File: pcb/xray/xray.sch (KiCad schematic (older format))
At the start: 5 parts, among them J1 Raspberry_Pi_2_3, M1 Nema17

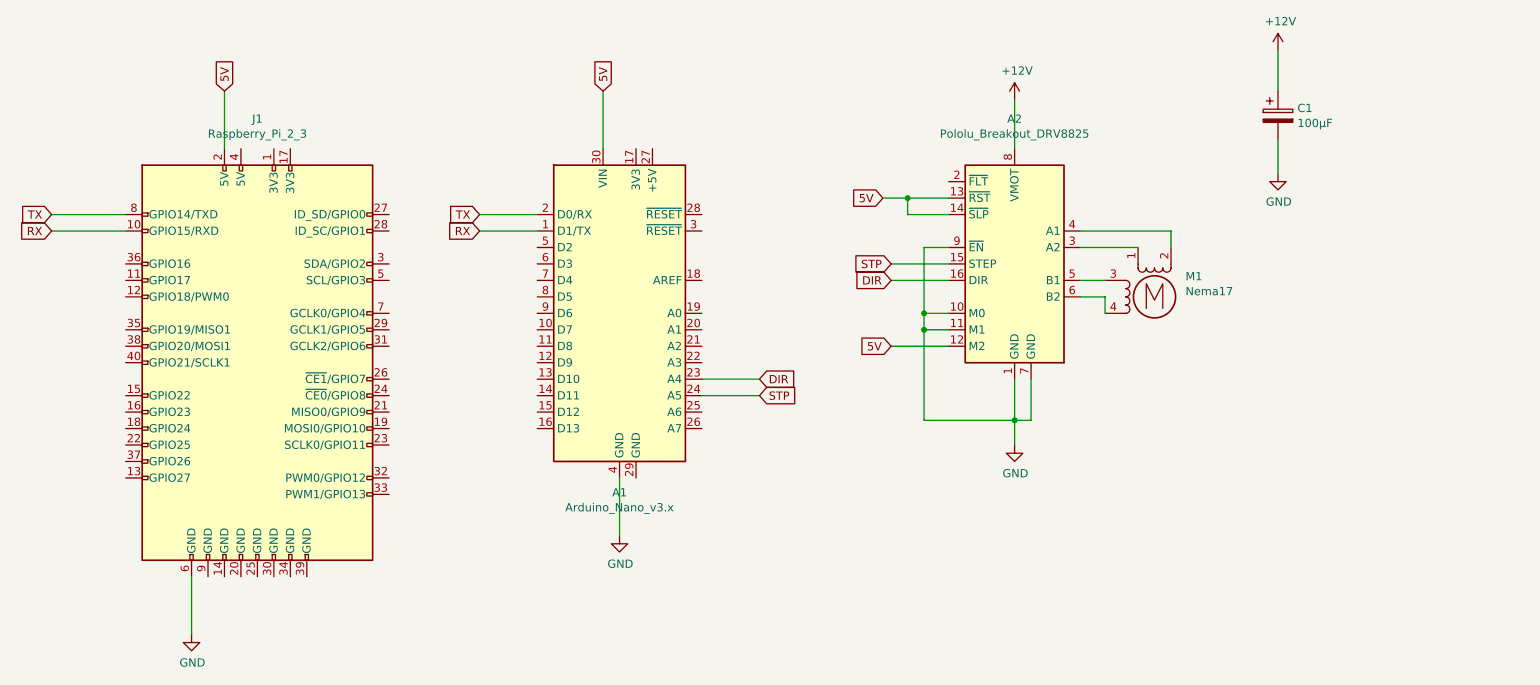
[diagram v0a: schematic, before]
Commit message: Add Schematic
Updated schematic using an Arduino pro micro or Leonardo
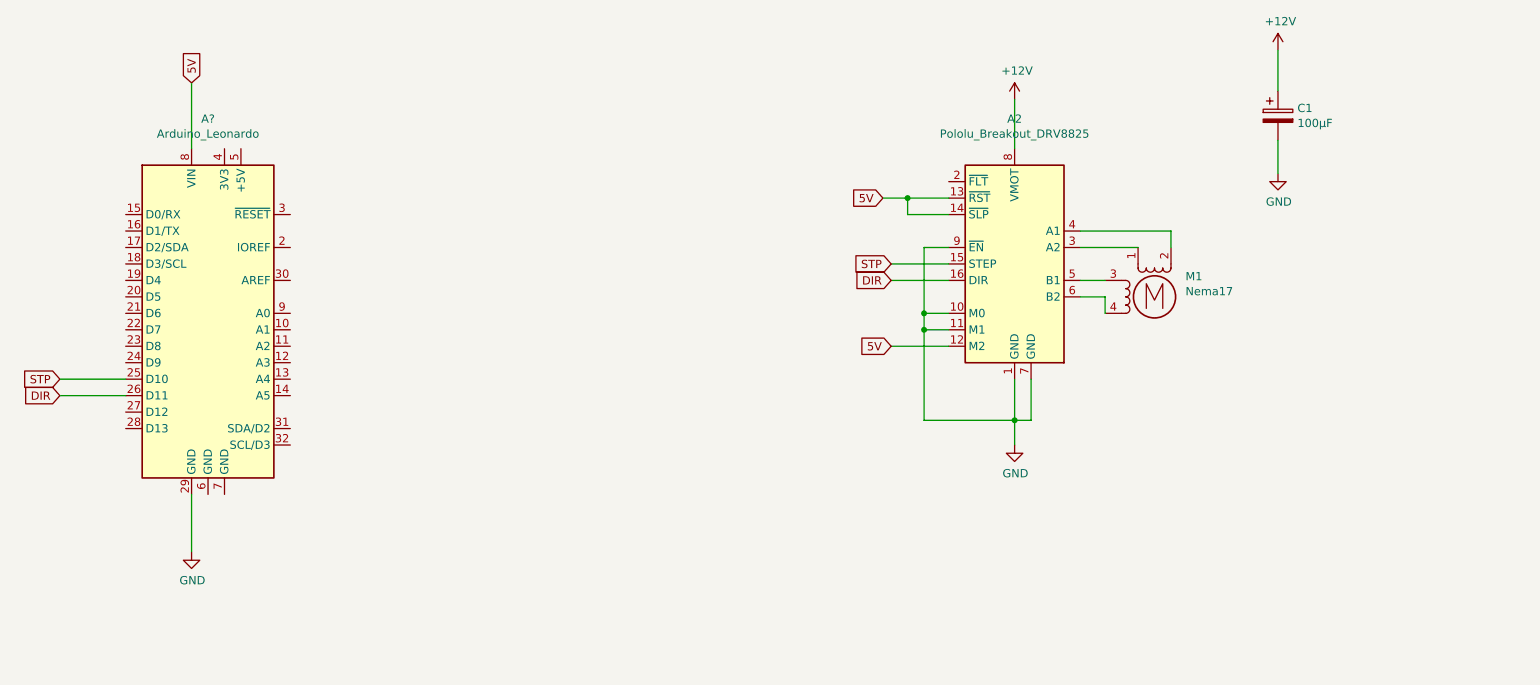
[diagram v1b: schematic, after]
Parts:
- removed A1: Arduino_Nano_v3.x, Module:Arduino_Nano, symbol MCU_Module:Arduino_Nano_v3.x
- removed J1: Raspberry_Pi_2_3, symbol Connector:Raspberry_Pi_2_3
- added A?: Arduino_Leonardo, Module:Arduino_UNO_R3, symbol MCU_Module:Arduino_Leonardo
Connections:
- net 5V: now also A?.8 (VIN)
- net DIR: now also A?.26 (D11)
- net GND: now also A?.29 (GND)
- net STP: now also A?.25 (D10)
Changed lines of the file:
@@
 $EndDescr
-$Comp
-L MCU_Module:Arduino_Nano_v3.x A1
-U 1 1 5E1B5952
-P 4400 2400
-F 0 "A1" H 4400 1311 50  0000 C CNN
-F 1 "Arduino_Nano_v3.x" H 4400 1220 50  0000 C CNN
-F 2 "Module:Arduino_Nano" H 4400 2400 50  0001 C CIN
-F 3 "http://www.mouser.com/pdfdocs/Gravitech_Arduino_Nano3_0.pdf" H 4400 2400 50  0001 C CNN
-	1    4400 2400
-	1    0    0    -1
-$EndComp
-$Comp
-L Connector:Raspberry_Pi_2_3 J1
-U 1 1 5E1B8D85
-P 2200 2700
-F 0 "J1" H 2200 4181 50  0000 C CNN
-F 1 "Raspberry_Pi_2_3" H 2200 4090 50  0000 C CNN
-F 2 "" H 2200 2700 50  0001 C CNN
-F 3 "https://www.raspberrypi.org/documentation/hardware/raspberrypi/schematics/rpi_SCH_3bplus_1p0_reduced.pdf" H 2200 2700 50  0001 C CNN
-	1    2200 2700
-	1    0    0    -1
-$EndComp
 $Comp
 L Device:CP C1
@@
 	1    0    0    -1
 $EndComp
-Text GLabel 2000 1050 1    50   Input ~ 0
-5V
-Text GLabel 950  1800 0    50   Input ~ 0
-TX
-Text GLabel 950  1900 0    50   Input ~ 0
-RX
-Wire Wire Line
-	2000 1400 2000 1050
-Wire Wire Line
-	1400 1800 950  1800
-Wire Wire Line
-	1800 4350 1800 4000
-$Comp
-L power:GND #PWR?
-U 1 1 5E21297F
-P 1800 4350
-F 0 "#PWR?" H 1800 4100 50  0001 C CNN
-F 1 "GND" H 1805 4177 50  0000 C CNN
-F 2 "" H 1800 4350 50  0001 C CNN
-F 3 "" H 1800 4350 50  0001 C CNN
-	1    1800 4350
-	1    0    0    -1
-$EndComp
-$Comp
-L power:GND #PWR?
-U 1 1 5E214FEC
-P 4400 3750
-F 0 "#PWR?" H 4400 3500 50  0001 C CNN
-F 1 "GND" H 4405 3577 50  0000 C CNN
-F 2 "" H 4400 3750 50  0001 C CNN
-F 3 "" H 4400 3750 50  0001 C CNN
-	1    4400 3750
-	1    0    0    -1
-$EndComp
-Wire Wire Line
-	4400 3750 4400 3400
-Text GLabel 4300 1050 1    50   Input ~ 0
-5V
-Text GLabel 3550 1900 0    50   Input ~ 0
-RX
-Text GLabel 3550 1800 0    50   Input ~ 0
-TX
-Wire Wire Line
-	4300 1050 4300 1400
 $Comp
 L power:GND #PWR?
@@
 	1    0    0    -1
 $EndComp
-Wire Wire Line
-	950  1900 1400 1900
-Wire Wire Line
-	3550 1900 3900 1900
-Wire Wire Line
-	3550 1800 3900 1800
-Text GLabel 5250 2800 2    50   Input ~ 0
-DIR
-Text GLabel 5250 2900 2    50   Input ~ 0
-STP
-Wire Wire Line
-	4900 2800 5250 2800
-Wire Wire Line
-	5250 2900 4900 2900
 Text GLabel 6050 2200 0    50   Input ~ 0
 DIR
@@
 Wire Wire Line
 	7750 1900 7200 1900
+$Comp
+L MCU_Module:Arduino_Leonardo A?
+U 1 1 5E1C1CEB
+P 1900 2400
+F 0 "A?" H 1900 3581 50  0000 C CNN
+F 1 "Arduino_Leonardo" H 1900 3490 50  0000 C CNN
+F 2 "Module:Arduino_UNO_R3" H 1900 2400 50  0001 C CIN
+F 3 "https://www.arduino.cc/en/Main/ArduinoBoardLeonardo" H 1900 2400 50  0001 C CNN
+	1    1900 2400
+	1    0    0    -1
+$EndComp
+Text GLabel 1800 1000 1    50   Input ~ 0
+5V
+$Comp
+L power:GND #PWR?
+U 1 1 5E1C79C8
+P 1800 3850
+F 0 "#PWR?" H 1800 3600 50  0001 C CNN
+F 1 "GND" H 1805 3677 50  0000 C CNN
+F 2 "" H 1800 3850 50  0001 C CNN
+F 3 "" H 1800 3850 50  0001 C CNN
+	1    1800 3850
+	1    0    0    -1
+$EndComp
+Text GLabel 1000 2900 0    50   Input ~ 0
+DIR
+Text GLabel 1000 2800 0    50   Input ~ 0
+STP
+Wire Wire Line
+	1000 2800 1400 2800
+Wire Wire Line
+	1400 2900 1000 2900
+Wire Wire Line
+	1800 3850 1800 3500
+Wire Wire Line
+	1800 1000 1800 1400
 $EndSCHEMATC

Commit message: Update schematic
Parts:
- removed A?: Arduino_Leonardo, Module:Arduino_UNO_R3, symbol MCU_Module:Arduino_Leonardo
- added MCU1: Arduino_Micro, xray:Arduino_Micro, symbol xray:Arduino_Micro
- C1: footprint (none) -> Capacitor_THT:C_Radial_D5.0mm_H11.0mm_P2.00mm
- M1: footprint (none) -> Connector_PinHeader_2.54mm:PinHeader_1x04_P2.54mm_Vertical
- renumbered A2 to StepperDriver1
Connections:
- net 5V: now also MCU1.12 (5V)
- net DIR: now also MCU1.8 (PF1)
- net GND: now also MCU1.14 (GND)
- net STP: now also MCU1.9 (PF0)
- no-connect marks 0 -> 29
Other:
- moved on the sheet: C1
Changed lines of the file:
@@
 L Device:CP C1
 U 1 1 5E1C1B73
-P 8400 1200
-F 0 "C1" H 8518 1246 50  0000 L CNN
-F 1 "100µF" H 8518 1155 50  0000 L CNN
-F 2 "" H 8438 1050 50  0001 C CNN
-F 3 "~" H 8400 1200 50  0001 C CNN
-	1    8400 1200
-	1    0    0    -1
-$EndComp
-$Comp
-L power:GND #PWR?
+P 9500 2000
+F 0 "C1" H 9618 2046 50  0000 L CNN
+F 1 "100µF" H 9618 1955 50  0000 L CNN
+F 2 "Capacitor_THT:C_Radial_D5.0mm_H11.0mm_P2.00mm" H 9538 1850 50  0001 C CNN
+F 3 "~" H 9500 2000 50  0001 C CNN
+	1    9500 2000
+	1    0    0    -1
+$EndComp
+$Comp
+L power:GND #PWR0101
 U 1 1 5E228E9B
-P 8400 1550
-F 0 "#PWR?" H 8400 1300 50  0001 C CNN
-F 1 "GND" H 8405 1377 50  0000 C CNN
-F 2 "" H 8400 1550 50  0001 C CNN
-F 3 "" H 8400 1550 50  0001 C CNN
-	1    8400 1550
-	1    0    0    -1
-$EndComp
-$Comp
-L power:+12V #PWR?
+P 9500 2350
+F 0 "#PWR0101" H 9500 2100 50  0001 C CNN
+F 1 "GND" H 9505 2177 50  0000 C CNN
+F 2 "" H 9500 2350 50  0001 C CNN
+F 3 "" H 9500 2350 50  0001 C CNN
+	1    9500 2350
+	1    0    0    -1
+$EndComp
+$Comp
+L power:+12V #PWR0102
 U 1 1 5E22ACB5
-P 8400 800
-F 0 "#PWR?" H 8400 650 50  0001 C CNN
-F 1 "+12V" H 8415 973 50  0000 C CNN
-F 2 "" H 8400 800 50  0001 C CNN
-F 3 "" H 8400 800 50  0001 C CNN
-	1    8400 800
-	1    0    0    -1
-$EndComp
-Wire Wire Line
-	8400 1550 8400 1350
-Wire Wire Line
-	8400 1050 8400 800
+P 9500 1600
+F 0 "#PWR0102" H 9500 1450 50  0001 C CNN
+F 1 "+12V" H 9515 1773 50  0000 C CNN
+F 2 "" H 9500 1600 50  0001 C CNN
+F 3 "" H 9500 1600 50  0001 C CNN
+	1    9500 1600
+	1    0    0    -1
+$EndComp
+Wire Wire Line
+	9500 2350 9500 2150
+Wire Wire Line
+	9500 1850 9500 1600
 Wire Wire Line
 	6800 1400 6800 1100
 $Comp
-L power:+12V #PWR?
+L power:+12V #PWR0103
 U 1 1 5E22B94A
 P 6800 1100
-F 0 "#PWR?" H 6800 950 50  0001 C CNN
+F 0 "#PWR0103" H 6800 950 50  0001 C CNN
 F 1 "+12V" H 6815 1273 50  0000 C CNN
 F 2 "" H 6800 1100 50  0001 C CNN
@@
 	6800 3050 6800 2800
 $Comp
-L power:GND #PWR?
+L power:GND #PWR0104
 U 1 1 5E217E33
 P 6800 3200
-F 0 "#PWR?" H 6800 2950 50  0001 C CNN
+F 0 "#PWR0104" H 6800 2950 50  0001 C CNN
 F 1 "GND" H 6805 3027 50  0000 C CNN
 F 2 "" H 6800 3200 50  0001 C CNN
@@
 	6250 2500 6250 3050
 $Comp
-L Driver_Motor:Pololu_Breakout_DRV8825 A2
+L Driver_Motor:Pololu_Breakout_DRV8825 StepperDriver1
 U 1 1 5E1E22D3
 P 6800 2000
-F 0 "A2" H 6800 2781 50  0000 C CNN
+F 0 "StepperDriver1" H 6800 2781 50  0000 C CNN
 F 1 "Pololu_Breakout_DRV8825" H 6800 2690 50  0000 C CNN
 F 2 "Module:Pololu_Breakout-16_15.2x20.3mm" H 7000 1200 50  0001 L CNN
@@
 F 0 "M1" H 7838 2424 50  0000 L CNN
 F 1 "Nema17" H 7838 2333 50  0000 L CNN
-F 2 "" H 7660 2290 50  0001 C CNN
+F 2 "Connector_PinHeader_2.54mm:PinHeader_1x04_P2.54mm_Vertical" H 7660 2290 50  0001 C CNN
 F 3 "" H 7660 2290 50  0001 C CNN
 	1    7650 2300
@@
 Wire Wire Line
 	7750 1900 7200 1900
-$Comp
-L MCU_Module:Arduino_Leonardo A?
-U 1 1 5E1C1CEB
-P 1900 2400
-F 0 "A?" H 1900 3581 50  0000 C CNN
-F 1 "Arduino_Leonardo" H 1900 3490 50  0000 C CNN
-F 2 "Module:Arduino_UNO_R3" H 1900 2400 50  0001 C CIN
-F 3 "https://www.arduino.cc/en/Main/ArduinoBoardLeonardo" H 1900 2400 50  0001 C CNN
-	1    1900 2400
-	1    0    0    -1
-$EndComp
-Text GLabel 1800 1000 1    50   Input ~ 0
+Text GLabel 3500 1100 1    50   Input ~ 0
 5V
 $Comp
-L power:GND #PWR?
+L power:GND #PWR0105
 U 1 1 5E1C79C8
-P 1800 3850
-F 0 "#PWR?" H 1800 3600 50  0001 C CNN
-F 1 "GND" H 1805 3677 50  0000 C CNN
-F 2 "" H 1800 3850 50  0001 C CNN
-F 3 "" H 1800 3850 50  0001 C CNN
-	1    1800 3850
-	1    0    0    -1
-$EndComp
-Text GLabel 1000 2900 0    50   Input ~ 0
+P 3450 3550
+F 0 "#PWR0105" H 3450 3300 50  0001 C CNN
+F 1 "GND" H 3455 3377 50  0000 C CNN
+F 2 "" H 3450 3550 50  0001 C CNN
+F 3 "" H 3450 3550 50  0001 C CNN
+	1    3450 3550
+	1    0    0    -1
+$EndComp
+Text GLabel 4350 2750 2    50   Input ~ 0
 DIR
-Text GLabel 1000 2800 0    50   Input ~ 0
+Text GLabel 4350 2900 2    50   Input ~ 0
 STP
-Wire Wire Line
-	1000 2800 1400 2800
-Wire Wire Line
-	1400 2900 1000 2900
-Wire Wire Line
-	1800 3850 1800 3500
-Wire Wire Line
-	1800 1000 1800 1400
+NoConn ~ 6400 1600
+$Comp
+L xray:Arduino_Micro MCU1
+U 1 1 5E56E302
+P 3350 1800
+F 0 "MCU1" V 3500 1250 50  0000 C CNN
+F 1 "Arduino_Micro" V 3600 1250 50  0000 C CNN
+F 2 "xray:Arduino_Micro" H 3400 2400 50  0001 C CNN
+F 3 "" H 3400 2400 50  0001 C CNN
+	1    3350 1800
+	1    0    0    -1
+$EndComp
+Wire Wire Line
+	4200 2750 4200 2800
+Wire Wire Line
+	4200 2800 4050 2800
+Wire Wire Line
+	4200 2750 4350 2750
+Wire Wire Line
+	4350 2900 4050 2900
+Wire Wire Line
+	3450 3200 3450 3550
+Wire Wire Line
+	3500 1100 3500 1450
+NoConn ~ 3000 1700
+NoConn ~ 3400 1450
+NoConn ~ 3600 1450
+NoConn ~ 4050 1700
+NoConn ~ 4050 1800
+NoConn ~ 4050 1900
+NoConn ~ 4050 2000
+NoConn ~ 4050 2100
+NoConn ~ 4050 2200
+NoConn ~ 4050 2300
+NoConn ~ 4050 2400
+NoConn ~ 4050 2500
+NoConn ~ 4050 2600
+NoConn ~ 4050 2700
+NoConn ~ 3550 3200
+NoConn ~ 3000 3000
+NoConn ~ 3000 2900
+NoConn ~ 3000 2800
+NoConn ~ 3000 2700
+NoConn ~ 3000 2600
+NoConn ~ 3000 2500
+NoConn ~ 3000 2400
+NoConn ~ 3000 2300
+NoConn ~ 3000 2200
+NoConn ~ 3000 2100
+NoConn ~ 3000 2000
+NoConn ~ 3000 1900
+NoConn ~ 3000 1800
 $EndSCHEMATC
